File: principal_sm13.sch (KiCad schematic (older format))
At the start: 3 parts

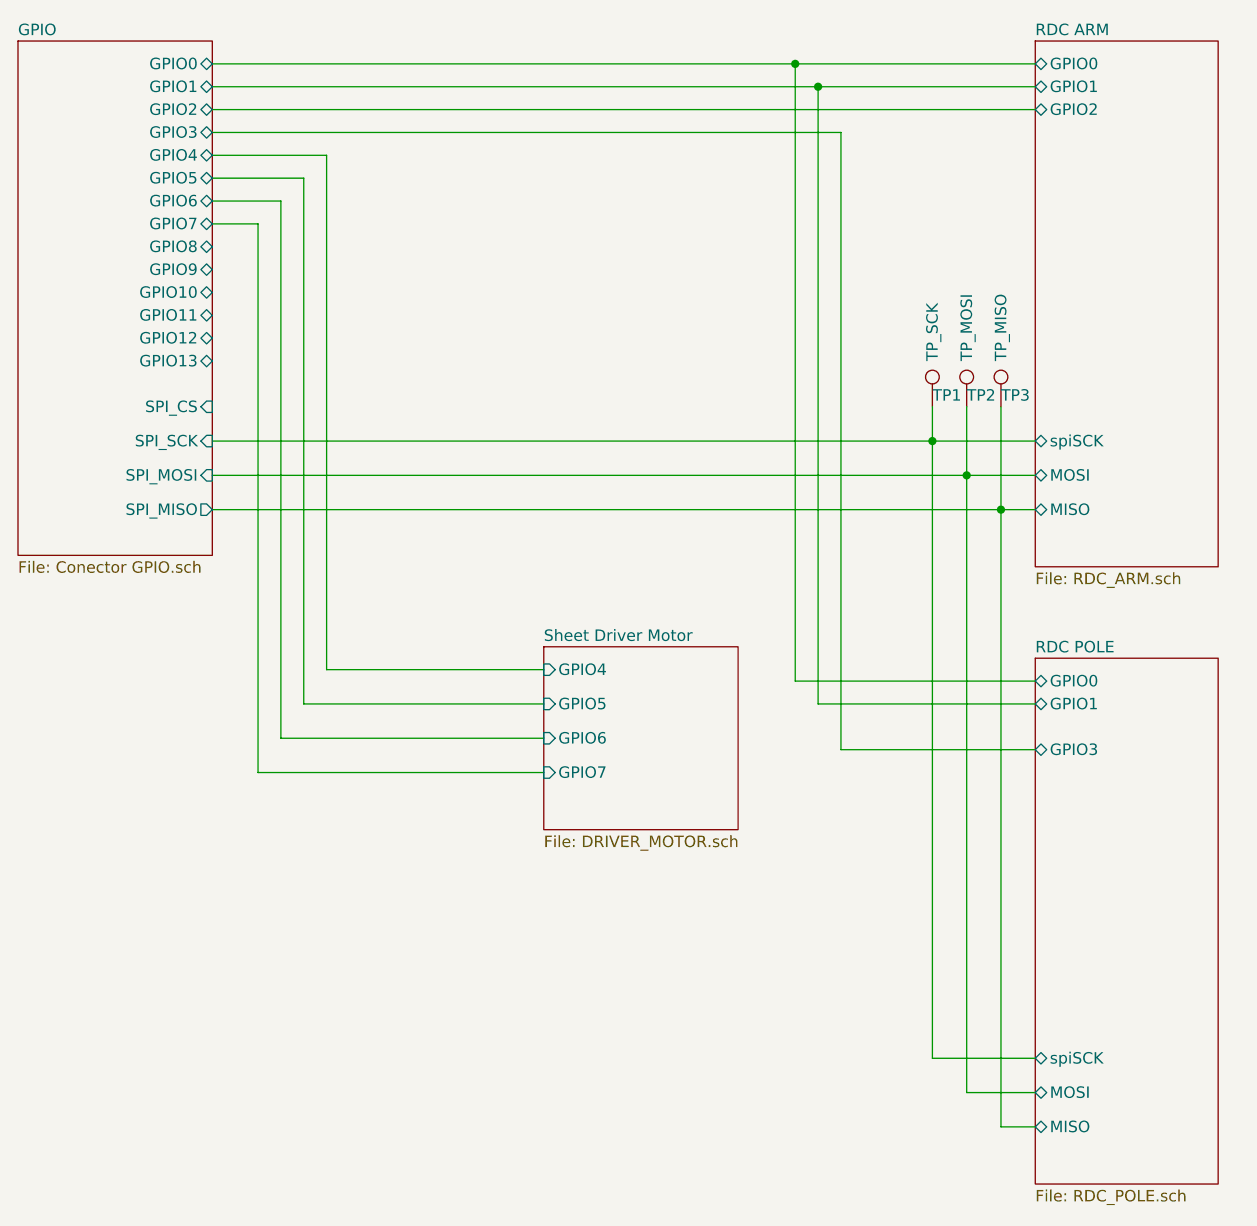
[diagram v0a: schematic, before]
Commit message: eliminado gpio para motores ya que la CIAA no cuenta con suficientes GPIOs disponibles. Se usara DOUTS
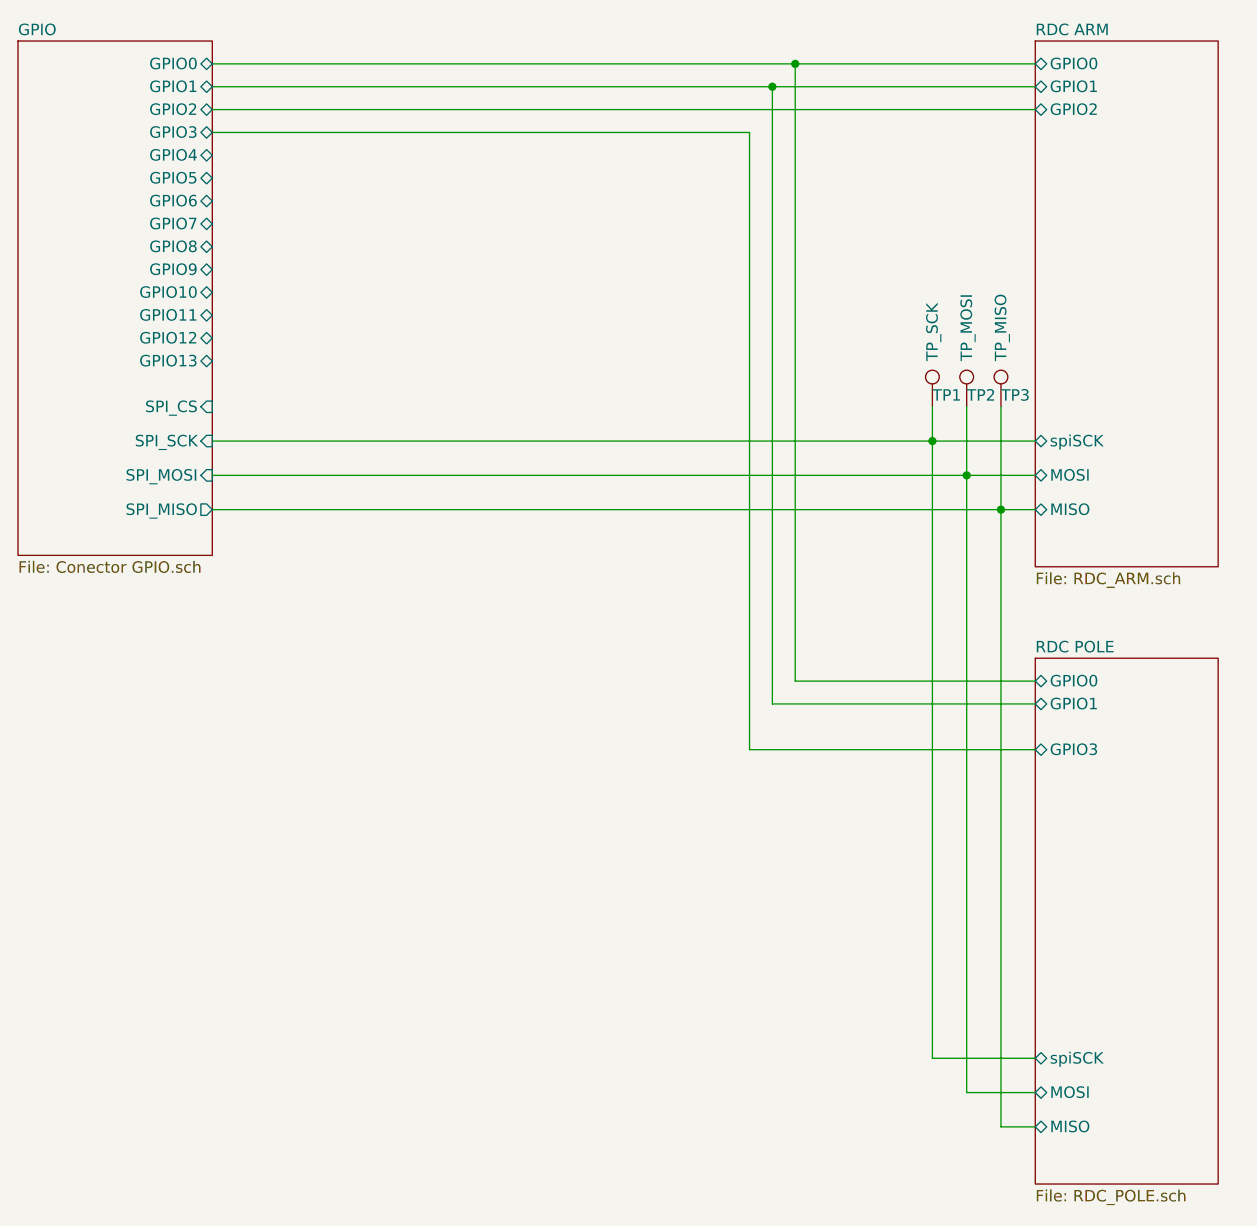
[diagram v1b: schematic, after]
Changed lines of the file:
@@
 $Descr A4 11693 8268
 encoding utf-8
-Sheet 1 5
+Sheet 1 4
 Title "RDC"
 Date "2020-06-22"
@@
 Wire Wire Line
 	6250 3800 7300 3800
-Wire Wire Line
-	6350 1200 6350 3900
-Connection ~ 6350 1200
-Wire Wire Line
-	6350 1200 7300 1200
-Wire Wire Line
-	6350 3900 7300 3900
 $Sheet
 S 7300 3700 800  2300
@@
 F7 "GPIO3" B L 7300 4100 50
 $EndSheet
-Wire Wire Line
-	6450 1400 6450 4100
-Wire Wire Line
-	6450 4100 7300 4100
 $Comp
 L Connector:TestPoint TP1
@@
 Wire Wire Line
 	7150 2600 7150 3050
-$Sheet
-S 5150 3650 850  800
-U 5F0E7624
-F0 "Sheet Driver Motor" 50
-F1 "DRIVER_MOTOR.sch" 50
-F2 "GPIO4" I L 5150 3750 50
-F3 "GPIO5" I L 5150 3900 50
-F4 "GPIO6" I L 5150 4050 50
-F5 "GPIO7" I L 5150 4200 50
-$EndSheet
-Wire Wire Line
-	3700 1500 4200 1500
-Wire Wire Line
-	4200 1500 4200 3750
-Wire Wire Line
-	4200 3750 5150 3750
-Wire Wire Line
-	3700 1600 4100 1600
-Wire Wire Line
-	4100 1600 4100 3900
-Wire Wire Line
-	4100 3900 5150 3900
-Wire Wire Line
-	4000 1700 4000 4050
 Wire Wire Line
 	3700 2750 6850 2750
@@
 	3700 3050 7150 3050
 Wire Wire Line
-	4000 4050 5150 4050
-Wire Wire Line
-	3700 1700 4000 1700
-Wire Wire Line
 	3700 1100 6250 1100
 Wire Wire Line
-	3700 1200 6350 1200
+	3700 1200 6150 1200
 Wire Wire Line
 	3700 1300 7300 1300
 Wire Wire Line
-	3700 1400 6450 1400
+	3700 1400 6050 1400
 Wire Wire Line
-	3700 1800 3900 1800
+	6050 4100 6050 1400
 Wire Wire Line
-	3900 1800 3900 4200
+	6150 3900 6150 1200
+Connection ~ 6150 1200
 Wire Wire Line
-	3900 4200 5150 4200
+	6150 1200 7300 1200
+Wire Wire Line
+	6150 3900 7300 3900
+Wire Wire Line
+	6050 4100 7300 4100
 $EndSCHEMATC

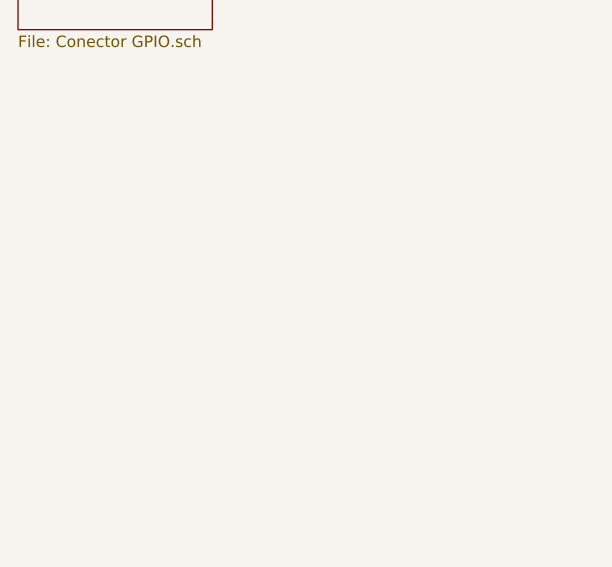
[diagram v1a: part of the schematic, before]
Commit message: Se arregló conexion erronea en los amplificadores operacionales
se agregó conexión 1-wire en GPIO8
se agregó botón y led que comparten GPIO7, la idea es leer el estado del
botón y al liberarlo cambiar el GPIO a output y encender el led indicando
alguna acción
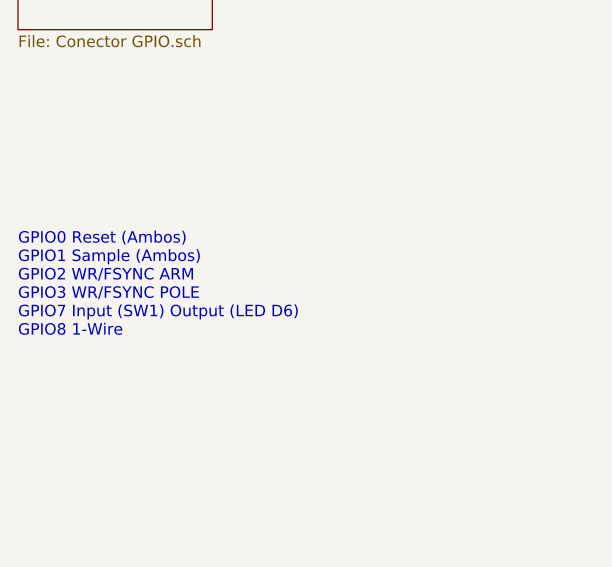
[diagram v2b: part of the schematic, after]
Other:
- note added: "GPIO0 Reset (Ambos)\nGPIO1 Sample (Ambos)\nGPIO2 WR/FSYNC ARM\nGPIO3 WR/FSYNC POLE\nGPIO7 Input (SW1) Output (LED D6)\nGPIO8 1-Wire\n"
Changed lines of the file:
@@
 Wire Wire Line
 	6050 4100 7300 4100
+Text Notes 2850 4600 0    50   ~ 0
+GPIO0 Reset (Ambos)\nGPIO1 Sample (Ambos)\nGPIO2 WR/FSYNC ARM\nGPIO3 WR/FSYNC POLE\nGPIO7 Input (SW1) Output (LED D6)\nGPIO8 1-Wire\n
 $EndSCHEMATC
